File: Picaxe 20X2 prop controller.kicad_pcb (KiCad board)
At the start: 2 copper layers, 100.6 x 83.2 mm, 64 parts, among them J1 FC68131, J10 Conn_01x05_Male (- power bus), J11 Conn_01x08_Male - pin I/O, J12 MP3 player, J13 servo 2, J14 servo 3, J15 servo 4, J16 servo 5, J17 Ext servo power, J18 Servo power select, J19 C.0, J2 Conn_01x08_Male - pin I/O, J20 C.5, J21 C.1, J22 C.6, J23 C.2, J24 C.7, J25 C.3, J26 C.4, J27 B.6 TX, J28 Screw_Terminal_01x06, J29 OSTTC020162, J3 servo 1, J4 servo 6, J5 B.7 RX, J6 OSTTC080162, J7 OSTTC020162, J8 PJ-202AH, J9 Conn_01x05_Male (+ power bus), U1 Picaxe 20X2, U3 L7805CV, U4 ULN2803A

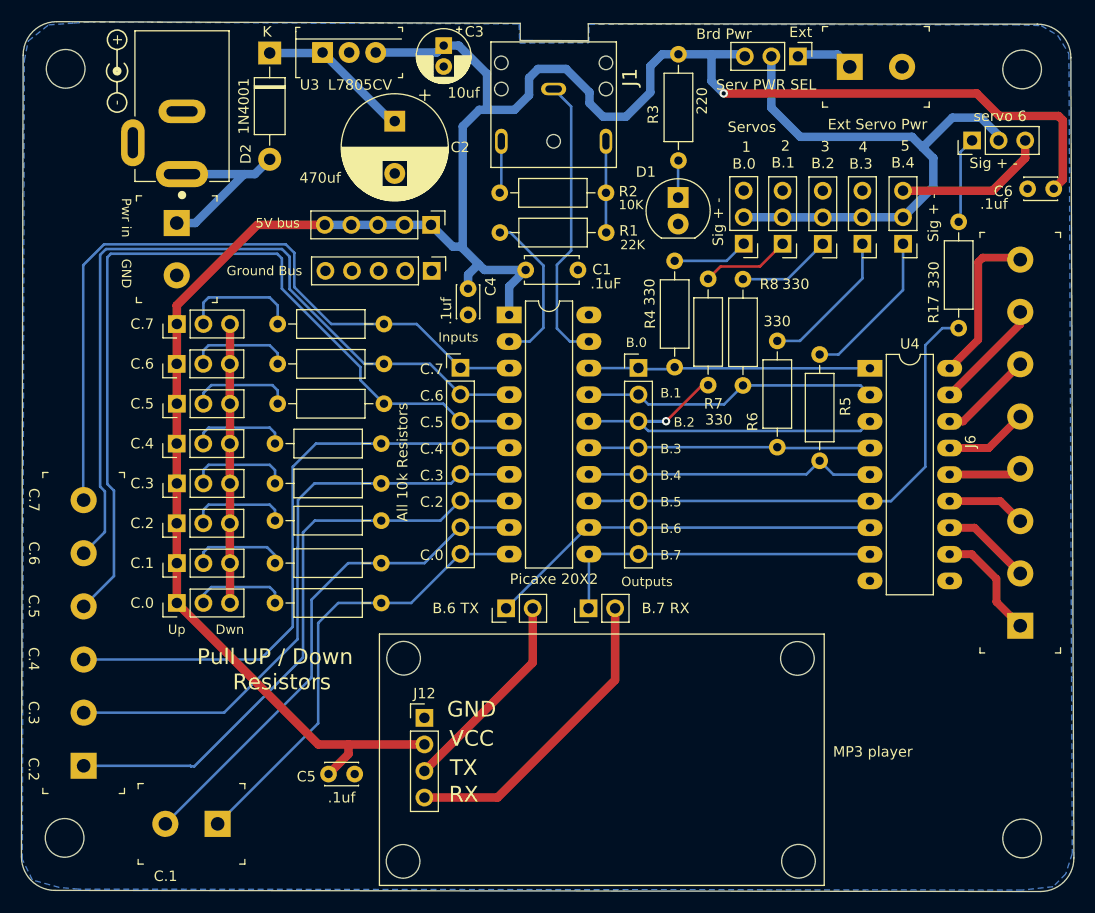
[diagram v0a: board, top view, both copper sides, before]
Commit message: added the 8 pin terminal block to the inputs
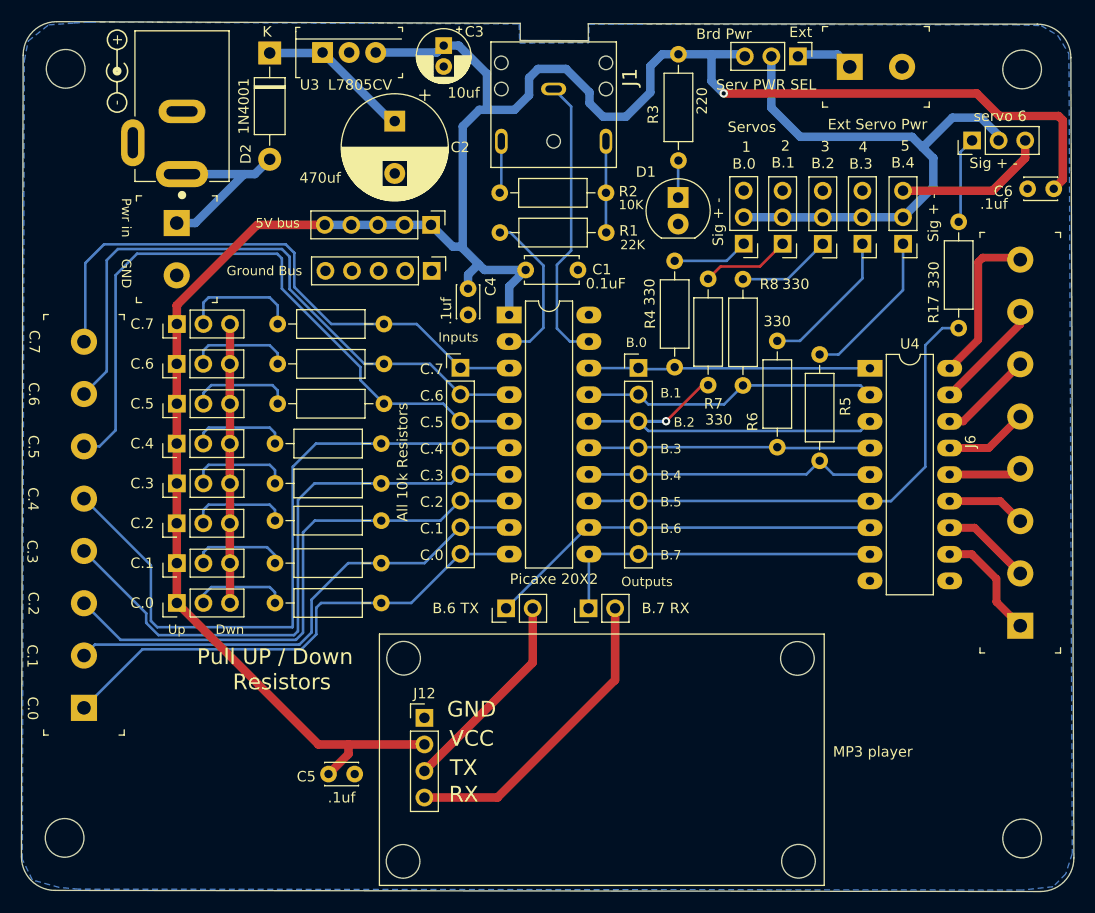
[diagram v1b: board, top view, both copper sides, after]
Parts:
- removed J29: OSTTC020162, digikey-footprints:Term_Block_1x2_P5mm
- C1: value .1uF -> 0.1uF
- J28: value Screw_Terminal_01x06 -> OSTTC080162; footprint digikey-footprints:Term_Block_1x6_P5.08mm -> digikey-footprints:Term_Block_1x8_P5mm
- moved J28 5.54 mm to (62.0, 133.0)
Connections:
- J28 pad 1: /ic2 -> /ic0
- J28 pad 2: /ic3 -> /ic1
- J28 pad 3: /ic4 -> /ic2
- J28 pad 4: /ic5 -> /ic3
- J28 pad 5: /ic6 -> /ic4
- J28 pad 6: /ic7 -> /ic5
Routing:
- net /ic5: track 82.4 -> 66.0 mm
- net /ic6: track 76.5 -> 60.2 mm
- net /ic7: track 70.8 -> 55.7 mm
- net /ic4: track 58.4 -> 65.3 mm
- net /ic2: track 58.2 -> 53.2 mm
- net /ic0: track 44.2 -> 48.3 mm
- net /ic1: track 49.0 -> 47.6 mm
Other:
- board text added: "C.0"
- board text added: "C.1"

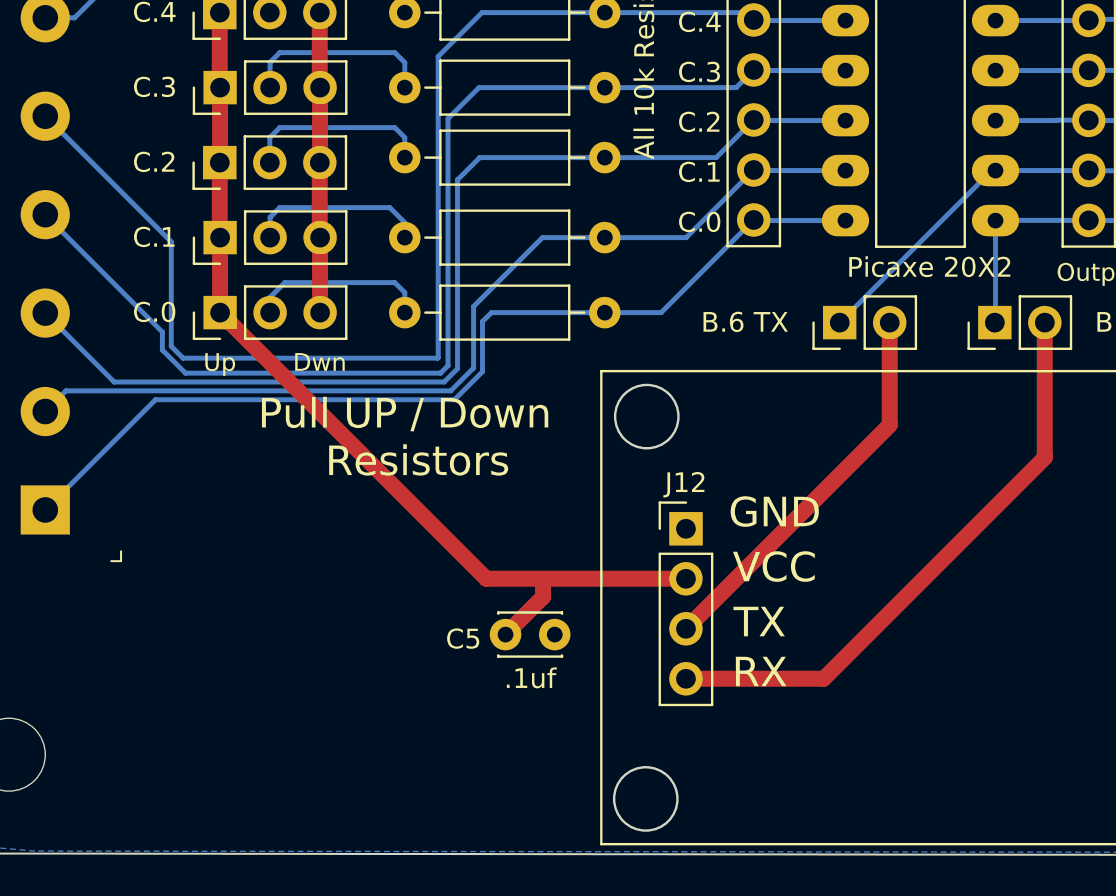
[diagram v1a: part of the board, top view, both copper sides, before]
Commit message: added a piezo and b.5 select jumper
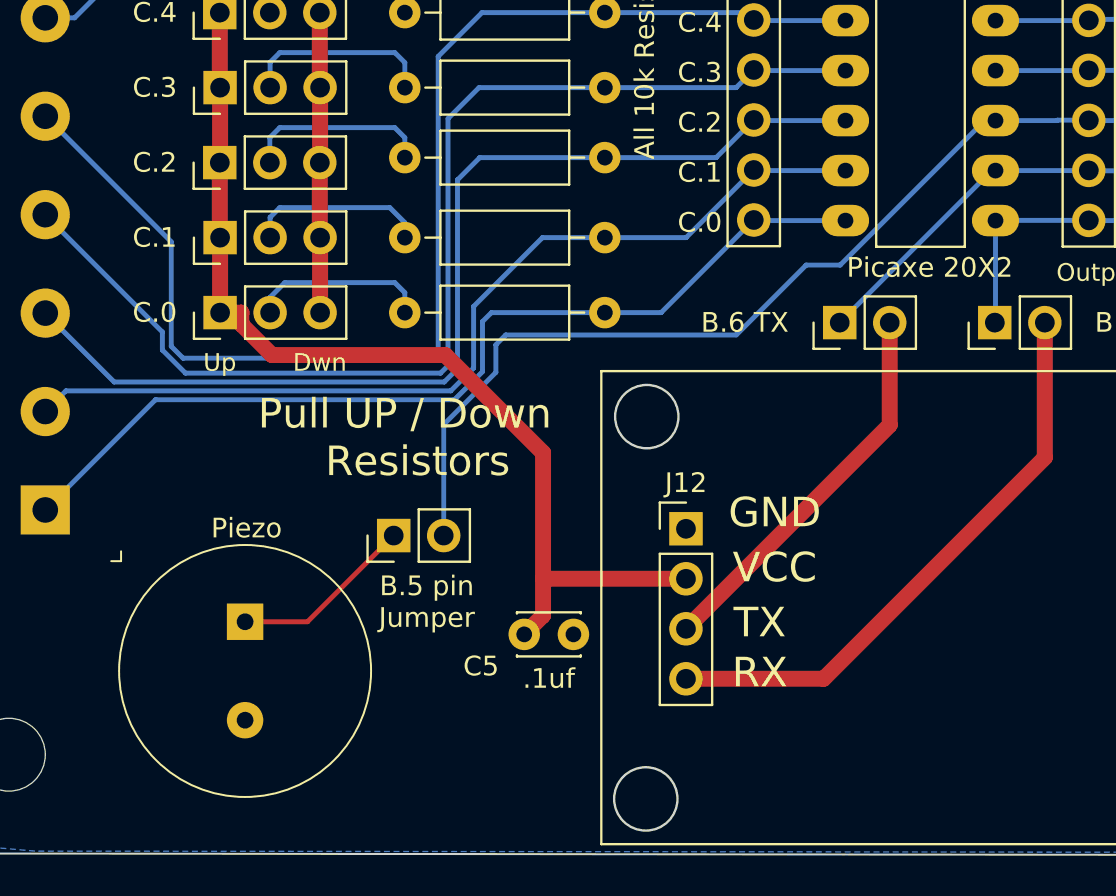
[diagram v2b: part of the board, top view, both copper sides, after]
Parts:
- added J29: B.5 pin, Connector_PinHeader_2.54mm:PinHeader_1x02_P2.54mm_Vertical, F.Cu at (79.7, 134.3)
- added Piezo: PS1240P02BT, digikey-footprints:Piezo_Transducer_THT_PS1240P02BT, F.Cu at (72.2, 138.6)
- moved C5 0.95 mm to (86.3, 139.3)
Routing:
- net /ob5: track 49.0 -> 89.9 mm
- net Net-(BZ1-Pad1): track 0.00 -> 9.36 mm
- net /5V: track 215.5 -> 219.2 mm
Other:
- board text added: "B.5 pin Jumper"

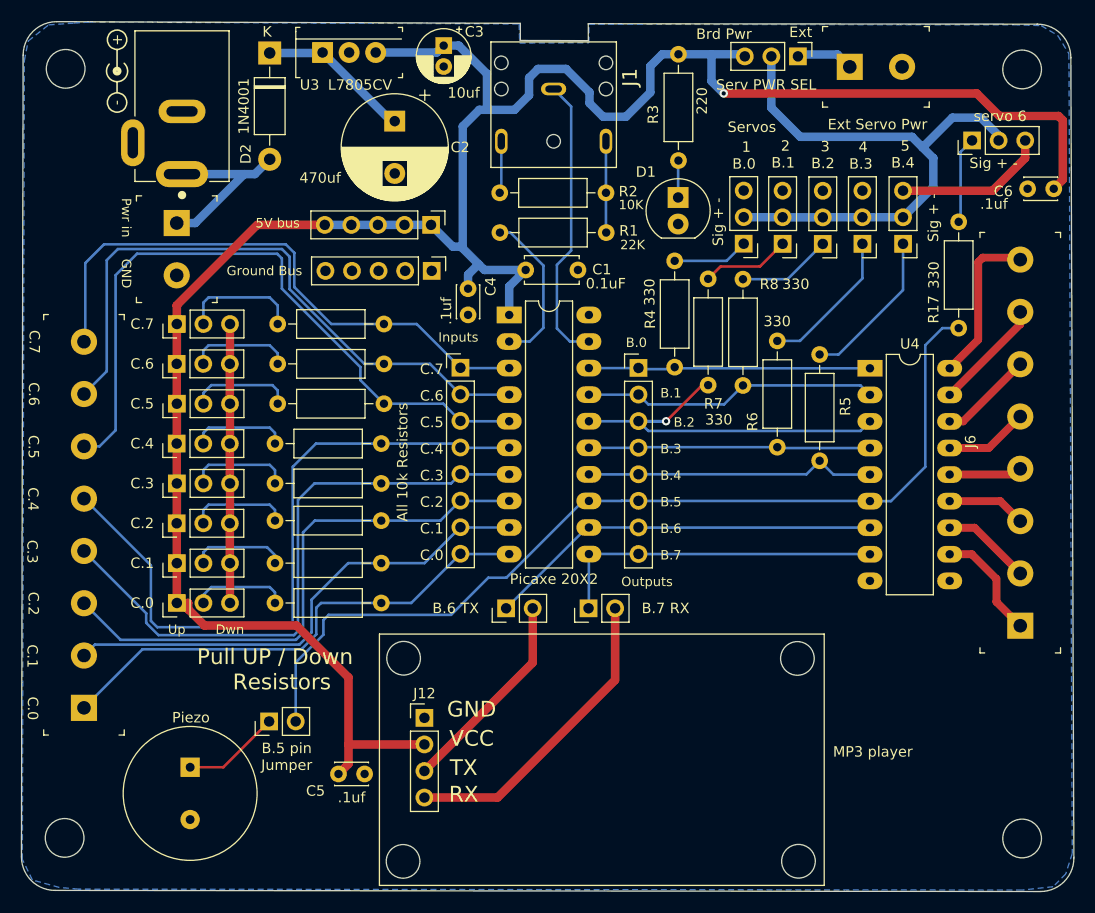
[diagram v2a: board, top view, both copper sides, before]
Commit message: Move 20X2 to Git
Will branch to see about moving the I2C connector
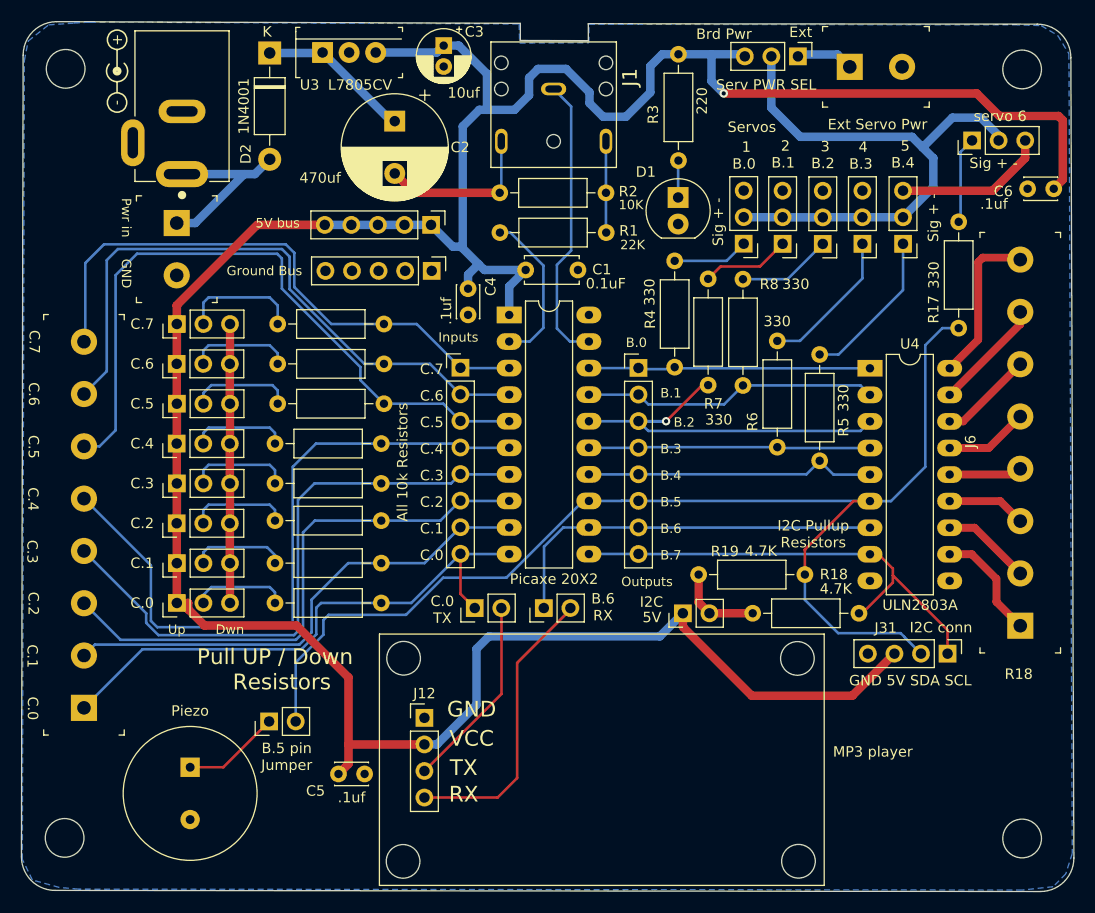
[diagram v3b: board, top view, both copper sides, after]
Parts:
- added J30: 5V, Connector_PinHeader_2.54mm:PinHeader_1x02_P2.54mm_Vertical, F.Cu at (119.3, 123.9)
- added J31: I2C conn, Connector_PinHeader_2.54mm:PinHeader_1x04_P2.54mm_Vertical, F.Cu at (144.6, 127.8)
- added R18: 4.7K, Resistor_THT:R_Axial_DIN0207_L6.3mm_D2.5mm_P10.16mm_Horizontal, F.Cu at (136.1, 123.9)
- added R19: 4.7K, Resistor_THT:R_Axial_DIN0207_L6.3mm_D2.5mm_P10.16mm_Horizontal, F.Cu at (120.8, 120.2)
- J27: value B.6 TX -> C.0 TX
- J5: value B.7 RX -> B.6 RX
- moved J5 4.28 mm to (106.0, 123.4)
- moved J27 3.00 mm to (99.4, 123.4)
- renumbered Piezo to Piezo1
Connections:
- J1 pad 2: Net-(J1-Pad2) -> GNDREF
- J27 pad 1: /ob6 -> /ic0
- J5 pad 1: /ob7 -> /ob6
- R2 pad 2: Net-(J1-Pad2) -> GNDREF
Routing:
- net /5V: track 219.2 -> 278.1 mm
- net /ob5: track 89.9 -> 116.1 mm
- net GNDREF: track 41.4 -> 57.2 mm
- net /ob7: track 32.1 -> 45.1 mm
- net Net-(J30-Pad2): track 0.00 -> 8.26 mm
- net /ic0: track 48.3 -> 54.0 mm
- net Net-(J1-Pad2): track 4.99 -> 0.00 mm
- net /RX: track 29.7 -> 28.0 mm
- net /TX: track 19.8 -> 18.6 mm
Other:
- board text added: "B.6 RX"
- board text added: "C.0 TX"
- board text added: "GND 5V SDA SCL"
- board text added: "I2C"
- board text added: "I2C Pullup Resistors"

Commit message: Moved I2C connector and started to add a battery select
Created a branch to move the I2C connector
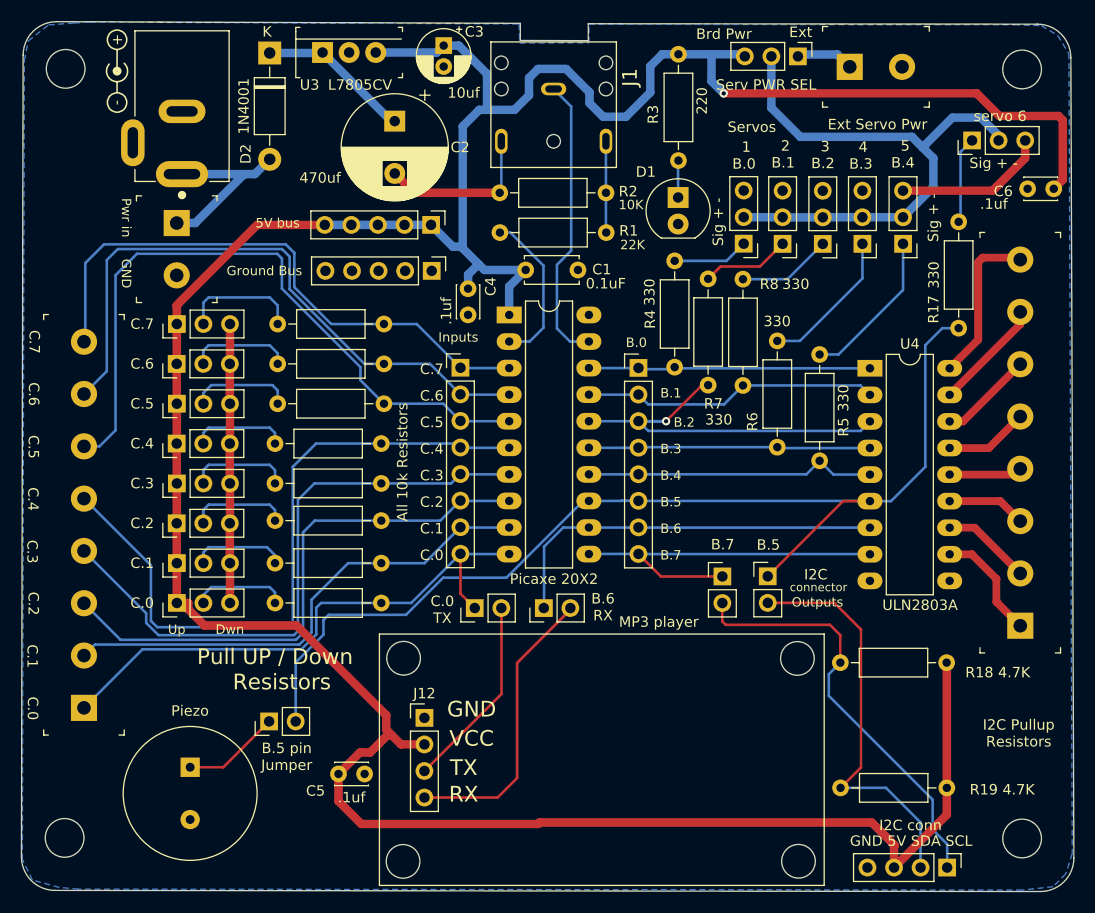
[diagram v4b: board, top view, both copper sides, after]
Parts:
- added J32: B.5, Connector_PinHeader_2.54mm:PinHeader_1x02_P2.54mm_Vertical, F.Cu at (127.4, 120.4)
- J27: value C.0 TX -> B.6 TX
- J30: value 5V -> B.7
- J5: value B.6 RX -> B.7 RX
- R18: value 4.7K -> R18 4.7K
- R19: value 4.7K -> R19 4.7K
- moved R19 31.3 mm to (144.5, 140.6), turned to 180 degrees
- moved J31 20.5 mm to (144.5, 148.2)
- moved J30 5.16 mm to (123.0, 120.4), turned to 0 degrees
- moved R18 5.04 mm to (134.3, 128.6), turned to 0 degrees
- moved G*** 2.50 mm to (143.5, 135.6)
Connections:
- J30 pad 1: /5V -> /ob7
- J30 pad 2: Net-(J30-Pad2) -> /I2CP1
- J31 pad 1: /ob7 -> /I2CP1
- J31 pad 2: /ob5 -> /I2CP2
- R18 pad 1: /ob7 -> /I2CP1
- R18 pad 2: Net-(J30-Pad2) -> /5V
- R19 pad 1: Net-(J30-Pad2) -> /5V
- R19 pad 2: /ob5 -> /I2CP2
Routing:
- net /I2CP1: track 0.00 -> 40.9 mm
- net /I2CP2: track 0.00 -> 39.2 mm
- net /5V: track 278.1 -> 301.1 mm
- net /ob5: track 116.1 -> 102.7 mm
- net /ob7: track 45.1 -> 35.8 mm
- net Net-(J30-Pad2): track 8.26 -> 0.00 mm
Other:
- board text added: "connector"

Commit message: Moved I2c connector and added battery select option
Added a battery connector and a select jumper to switch between the onboard regulator and the battery input connector. I also moved the I2C connector and added jumpers to disconnect the pins if needed.
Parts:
- added J33: Batt Connector, Connector_PinHeader_2.54mm:PinHeader_1x02_P2.54mm_Vertical, F.Cu at (61.9, 81.4)
- added J34: Batt in, Connector_PinHeader_2.54mm:PinHeader_1x03_P2.54mm_Vertical, F.Cu at (97.6, 77.1)
- J30: value B.7 -> B.6
- J32: value B.5 -> B.6
- R18: value R18 4.7K -> 4.7K
- R19: value R19 4.7K -> 4.7K
- moved C2 4.02 mm to (87.7, 77.0)
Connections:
- C3 pad 1: /5V -> /Reg out
- U3 pad 3: /5V -> /Reg out
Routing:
- net /Batt in: track 0.00 -> 44.7 mm
- net /Reg out: track 0.00 -> 18.5 mm
- net /5V: track 301.1 -> 286.8 mm
- net GNDREF: track 57.2 -> 61.8 mm
- net Net-(C2-Pad1): track 14.7 -> 12.8 mm
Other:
- board text added: "Batt Conn"
- board text added: "Pwr Sel"

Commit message: Added battery input polarity and changed 10uF to 2.4mm pin spacing
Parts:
- C3: footprint Capacitor_THT:CP_Radial_D5.0mm_P2.00mm -> Capacitor_THT:CP_Radial_D5.0mm_P2.50mm

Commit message: Board complete Beta test 1
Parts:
- added C7: .1uf, Capacitor_THT:C_Disc_D3.0mm_W2.0mm_P2.50mm, F.Cu at (147.0, 139.7)
- J30: value B.6 -> B.7
- J32: value B.6 -> B.5
- moved C4 6.04 mm to (97.9, 86.9)
- moved G*** 1.99 mm to (141.6, 135.1)
- moved J7 1.12 mm to (69.8, 86.6)
- moved J10 0.61 mm to (94.6, 91.2)
- moved J9 0.52 mm to (94.7, 86.8)
- moved C1 0.30 mm to (104.2, 91.4)
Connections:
- J29 pad 2: /ob5 -> /ob4
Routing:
- net /ob4: track 28.0 -> 72.8 mm
- net /ob5: track 102.7 -> 61.8 mm
- net /5V: track 286.8 -> 285.6 mm
- net VCC: track 17.4 -> 18.5 mm
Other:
- board text added: "B.4 pin Jumper"
- board text removed: "B.5 pin Jumper"
